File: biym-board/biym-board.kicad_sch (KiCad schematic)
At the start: 1 part

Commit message: Add driver external components
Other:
- sheet motor_driver ports: added ~{FAULT}; removed none
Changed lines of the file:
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@@
+    (stroke (width 0) (type default) (color 0 0 0 0))
+  )
+  (wire (pts (xy 217.17 100.33) (xy 214.63 100.33))
     (stroke (width 0) (type default) (color 0 0 0 0))
   )
@@
     (stroke (width 0) (type default) (color 0 0 0 0))
   )
+  (wire (pts (xy 182.88 102.87) (xy 180.34 102.87))
+    (stroke (width 0) (type default) (color 0 0 0 0))
+  )
   (wire (pts (xy 214.63 71.12) (xy 217.17 71.12))
     (stroke (width 0) (type default) (color 0 0 0 0))
@@
     (stroke (width 0) (type default) (color 0 0 0 0))
   )
+  (wire (pts (xy 180.34 113.03) (xy 182.88 113.03))
+    (stroke (width 0) (type default) (color 0 0 0 0))
+  )
   (wire (pts (xy 92.71 100.33) (xy 95.25 100.33))
     (stroke (width 0) (type default) (color 0 0 0 0))
@@
     (stroke (width 0) (type default) (color 0 0 0 0))
   )
+  (wire (pts (xy 180.34 105.41) (xy 182.88 105.41))
+    (stroke (width 0) (type default) (color 0 0 0 0))
+  )
   (wire (pts (xy 180.34 95.25) (xy 182.88 95.25))
     (stroke (width 0) (type default) (color 0 0 0 0))
@@
     (stroke (width 0) (type default) (color 0 0 0 0))
   )
+  (wire (pts (xy 180.34 107.95) (xy 182.88 107.95))
+    (stroke (width 0) (type default) (color 0 0 0 0))
+  )
   (wire (pts (xy 46.99 90.17) (xy 49.53 90.17))
     (stroke (width 0) (type default) (color 0 0 0 0))
@@
     (effects (font (size 1.27 1.27)) (justify right bottom))
   )
+  (label "DRIVER_PWM_A" (at 180.34 102.87 180)
+    (effects (font (size 1.27 1.27)) (justify right bottom))
+  )
   (label "GND" (at 46.99 95.25 180)
     (effects (font (size 1.27 1.27)) (justify right bottom))
@@
     (effects (font (size 1.27 1.27)) (justify right bottom))
   )
+  (label "~{DRIVER_FAULT}" (at 217.17 100.33 0)
+    (effects (font (size 1.27 1.27)) (justify left bottom))
+  )
   (label "VPERIPHERAL" (at 180.34 92.71 180)
     (effects (font (size 1.27 1.27)) (justify right bottom))
@@
     (effects (font (size 1.27 1.27)) (justify right bottom))
   )
+  (label "DRIVER_PWM_C" (at 180.34 107.95 180)
+    (effects (font (size 1.27 1.27)) (justify right bottom))
+  )
+  (label "DRIVER_PWM_B" (at 180.34 105.41 180)
+    (effects (font (size 1.27 1.27)) (justify right bottom))
+  )
   (label "~{DISABLE_ALL_POWER}" (at 95.25 100.33 0)
     (effects (font (size 1.27 1.27)) (justify left bottom))
+  )
+  (label "~{DRIVER_SLEEP}" (at 180.34 113.03 180)
+    (effects (font (size 1.27 1.27)) (justify right bottom))
   )
   (label "GND" (at 180.34 97.79 180)
@@
       (effects (font (size 1.27 1.27)) (justify left))
     )
-    (pin "PWM_B" input (at 182.88 102.87 180)
-      (effects (font (size 1.27 1.27)) (justify left))
-    )
-    (pin "PWM_A" input (at 182.88 105.41 180)
+    (pin "PWM_B" input (at 182.88 105.41 180)
+      (effects (font (size 1.27 1.27)) (justify left))
+    )
+    (pin "PWM_A" input (at 182.88 102.87 180)
       (effects (font (size 1.27 1.27)) (justify left))
     )
@@
     (pin "VDRIVER" passive (at 182.88 92.71 180)
       (effects (font (size 1.27 1.27)) (justify left))
+    )
+    (pin "~{FAULT}" output (at 214.63 100.33 0)
+      (effects (font (size 1.27 1.27)) (justify right))
     )
   )
@@
   )
   (symbol_instances
+    (path "/79116d11-26fd-48fc-b8f9-7a7b774125a1/2410a940-529b-42ac-a1a6-8eac39bf35e6"
+      (reference "C1") (unit 1) (value "0.1uF") (footprint "Janelia:SM0402")
+    )
+    (path "/79116d11-26fd-48fc-b8f9-7a7b774125a1/be9b6b49-dbbb-46e1-9161-07633a6035d9"
+      (reference "C2") (unit 1) (value "10uF") (footprint "Janelia:SM0402_POL")
+    )
+    (path "/79116d11-26fd-48fc-b8f9-7a7b774125a1/8a7cc49f-4666-4bff-88d8-7b1e5e0b9362"
+      (reference "C3") (unit 1) (value "0.1uF") (footprint "Janelia:SM0402")
+    )
+    (path "/79116d11-26fd-48fc-b8f9-7a7b774125a1/46ae94b0-5341-4bbb-afe7-3cf6a00b65a8"
+      (reference "C4") (unit 1) (value "0.1uF") (footprint "Janelia:SM0402")
+    )
+    (path "/79116d11-26fd-48fc-b8f9-7a7b774125a1/5df9f8b3-dc8a-4148-bf7f-d1adc6b6ce57"
+      (reference "C5") (unit 1) (value "10uF") (footprint "Janelia:SM0402_POL")
+    )
+    (path "/79116d11-26fd-48fc-b8f9-7a7b774125a1/a59ccd6c-12e8-44c6-9ed8-d91c4b04dd9f"
+      (reference "C6") (unit 1) (value "1uF") (footprint "Janelia:SM0402_POL")
+    )
+    (path "/79116d11-26fd-48fc-b8f9-7a7b774125a1/a44a33f9-40db-4e01-b1fe-0dfc38ff2344"
+      (reference "C7") (unit 1) (value "0.1uF") (footprint "Janelia:SM0402")
+    )
     (path "/78609776-14fe-41ec-972c-2bdc49eac818"
       (reference "FW1") (unit 1) (value "FEATHERWING_nRF52_POGO_PINS") (footprint "Janelia:FEATHERWING_POGO_PINS")
@@
     )
     (path "/79116d11-26fd-48fc-b8f9-7a7b774125a1/73049e1e-00b1-4d86-b27f-13c3a3887bed"
-      (reference "J?") (unit 1) (value "HEADER_01X03_JST_PH_VERTICAL") (footprint "Janelia:JST_PH_B3B-PH-K_1x03_P2.00mm_Vertical")
+      (reference "J2") (unit 1) (value "HEADER_01X03_JST_PH_VERTICAL") (footprint "Janelia:JST_PH_B3B-PH-K_1x03_P2.00mm_Vertical")
     )
     (path "/2c398cb1-cb17-49ba-86d6-22731656ead9/ab142e9c-269c-4749-bf0a-3cc0397cc4cb"
@@
       (reference "R1") (unit 1) (value "100k") (footprint "Janelia:SM0402")
     )
+    (path "/79116d11-26fd-48fc-b8f9-7a7b774125a1/922d9998-9360-4d64-bf82-803eb9724700"
+      (reference "R2") (unit 1) (value "5.1k") (footprint "Janelia:SM0402")
+    )
     (path "/79116d11-26fd-48fc-b8f9-7a7b774125a1/da95f1b2-1af2-47f6-bf0e-981916e2aac9"
-      (reference "U?") (unit 1) (value "DRV8311H") (footprint "Janelia:WQFN-24-1EP_3x3mm_P0.4mm_EP1.9x1.9mm_ThermalVias")
-    )
-  )
+      (reference "U1") (unit 1) (value "DRV8311H") (footprint "Janelia:WQFN-24-1EP_3x3mm_P0.4mm_EP1.9x1.9mm_ThermalVias")
+    )
+  )

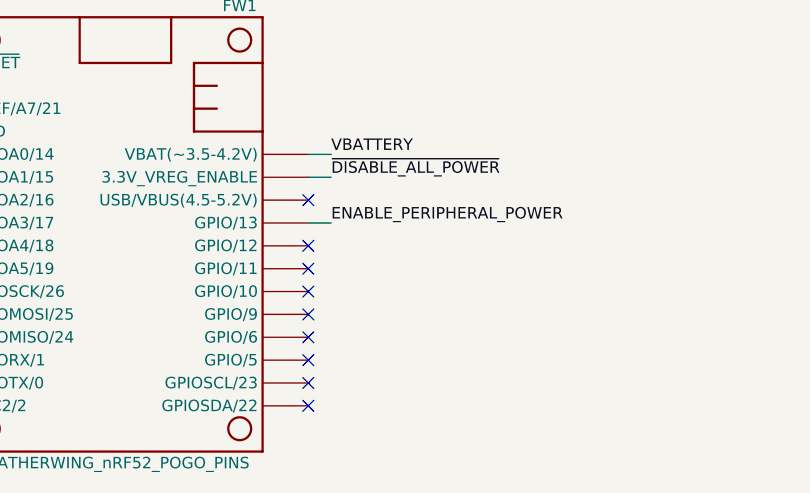
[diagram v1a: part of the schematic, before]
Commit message: Initial driver wiring
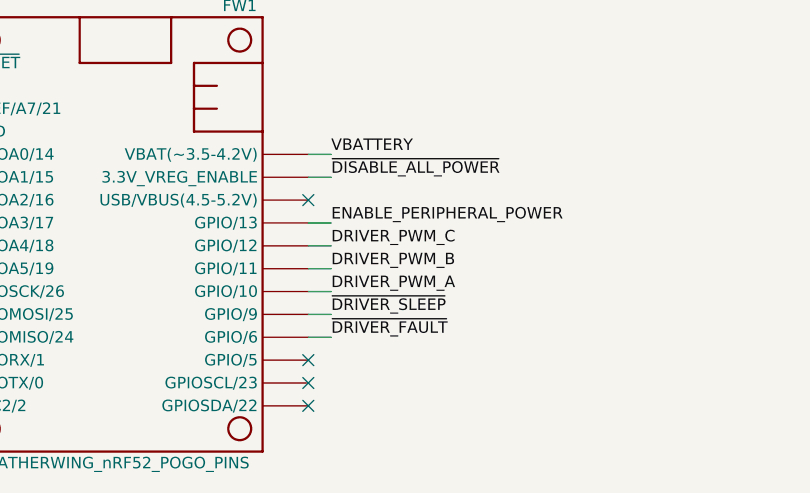
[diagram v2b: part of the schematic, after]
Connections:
- net DRIVER_PWM_A: now also FW1.22 (GPIO/10)
- net DRIVER_PWM_B: now also FW1.23 (GPIO/11)
- net DRIVER_PWM_C: now also FW1.24 (GPIO/12)
- net ~{DRIVER_FAULT}: now also FW1.20 (GPIO/6)
- net ~{DRIVER_SLEEP}: now also FW1.21 (GPIO/9)
- no-connect marks 23 -> 18
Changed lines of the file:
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@@
   (no_connect (at 49.53 92.71))
   (no_connect (at 49.53 123.19))
-  (no_connect (at 92.71 118.11))
   (no_connect (at 92.71 123.19))
   (no_connect (at 92.71 120.65))
@@
   (no_connect (at 49.53 87.63))
   (no_connect (at 49.53 113.03))
-  (no_connect (at 92.71 107.95))
-  (no_connect (at 92.71 110.49))
   (no_connect (at 49.53 120.65))
   (no_connect (at 49.53 105.41))
-  (no_connect (at 92.71 113.03))
   (no_connect (at 49.53 118.11))
   (no_connect (at 49.53 110.49))
-  (no_connect (at 92.71 115.57))
   (no_connect (at 92.71 102.87))
   (no_connect (at 49.53 102.87))
@@
     (stroke (width 0) (type default) (color 0 0 0 0))
   )
+  (wire (pts (xy 95.25 118.11) (xy 92.71 118.11))
+    (stroke (width 0) (type default) (color 0 0 0 0))
+  )
   (wire (pts (xy 92.71 105.41) (xy 95.25 105.41))
     (stroke (width 0) (type default) (color 0 0 0 0))
@@
     (stroke (width 0) (type default) (color 0 0 0 0))
   )
+  (wire (pts (xy 95.25 110.49) (xy 92.71 110.49))
+    (stroke (width 0) (type default) (color 0 0 0 0))
+  )
   (wire (pts (xy 214.63 71.12) (xy 217.17 71.12))
     (stroke (width 0) (type default) (color 0 0 0 0))
@@
     (stroke (width 0) (type default) (color 0 0 0 0))
   )
+  (wire (pts (xy 95.25 115.57) (xy 92.71 115.57))
+    (stroke (width 0) (type default) (color 0 0 0 0))
+  )
   (wire (pts (xy 180.34 105.41) (xy 182.88 105.41))
     (stroke (width 0) (type default) (color 0 0 0 0))
@@
     (stroke (width 0) (type default) (color 0 0 0 0))
   )
+  (wire (pts (xy 92.71 113.03) (xy 95.25 113.03))
+    (stroke (width 0) (type default) (color 0 0 0 0))
+  )
   (wire (pts (xy 180.34 107.95) (xy 182.88 107.95))
     (stroke (width 0) (type default) (color 0 0 0 0))
   )
+  (wire (pts (xy 92.71 107.95) (xy 95.25 107.95))
+    (stroke (width 0) (type default) (color 0 0 0 0))
+  )
   (wire (pts (xy 46.99 90.17) (xy 49.53 90.17))
     (stroke (width 0) (type default) (color 0 0 0 0))
   )
+  (label "~{DRIVER_FAULT}" (at 95.25 118.11 0)
+    (effects (font (size 1.27 1.27)) (justify left bottom))
+  )
   (label "ENABLE_PERIPHERAL_POWER" (at 95.25 105.41 0)
     (effects (font (size 1.27 1.27)) (justify left bottom))
@@
     (effects (font (size 1.27 1.27)) (justify right bottom))
   )
+  (label "DRIVER_PWM_B" (at 95.25 110.49 0)
+    (effects (font (size 1.27 1.27)) (justify left bottom))
+  )
   (label "GND" (at 46.99 95.25 180)
     (effects (font (size 1.27 1.27)) (justify right bottom))
@@
     (effects (font (size 1.27 1.27)) (justify right bottom))
   )
+  (label "DRIVER_PWM_C" (at 95.25 107.95 0)
+    (effects (font (size 1.27 1.27)) (justify left bottom))
+  )
+  (label "~{DRIVER_SLEEP}" (at 95.25 115.57 0)
+    (effects (font (size 1.27 1.27)) (justify left bottom))
+  )
   (label "~{DRIVER_FAULT}" (at 217.17 100.33 0)
     (effects (font (size 1.27 1.27)) (justify left bottom))
@@
   (label "VPERIPHERAL" (at 180.34 92.71 180)
     (effects (font (size 1.27 1.27)) (justify right bottom))
+  )
+  (label "DRIVER_PWM_A" (at 95.25 113.03 0)
+    (effects (font (size 1.27 1.27)) (justify left bottom))
   )
   (label "~{DISABLE_ALL_POWER}" (at 217.17 71.12 0)
@@
   )
   (symbol_instances
+    (path "/2c398cb1-cb17-49ba-86d6-22731656ead9/8e033e98-a73f-4e07-b564-ba8f1320f212"
+      (reference "#FLG0101") (unit 1) (value "PWR_FLAG") (footprint "")
+    )
     (path "/79116d11-26fd-48fc-b8f9-7a7b774125a1/2410a940-529b-42ac-a1a6-8eac39bf35e6"
       (reference "C1") (unit 1) (value "0.1uF") (footprint "Janelia:SM0402")

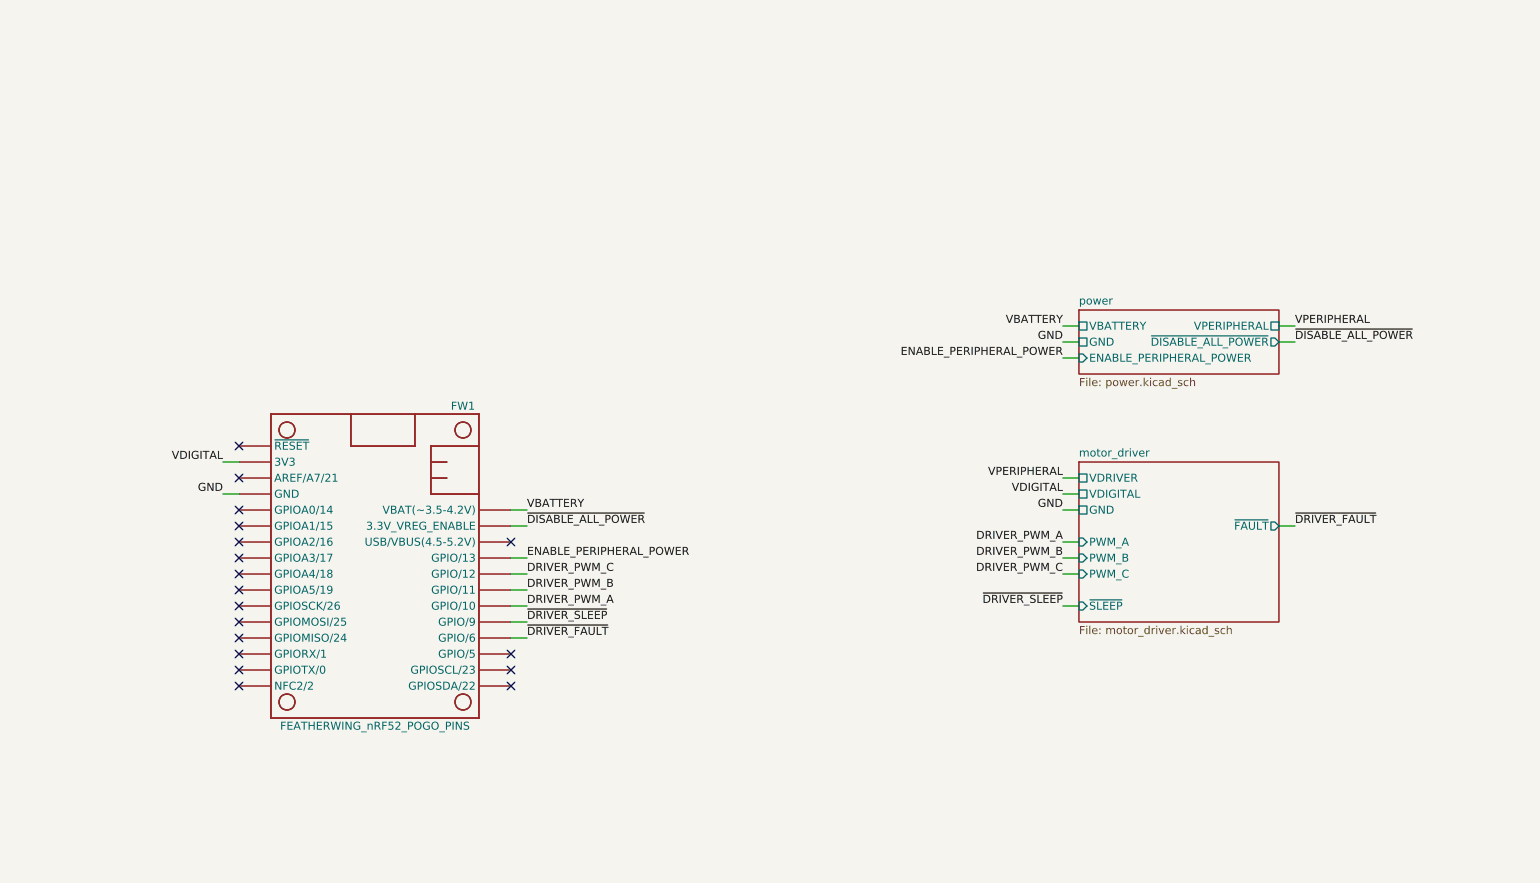
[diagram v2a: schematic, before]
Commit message: Add motor feedback
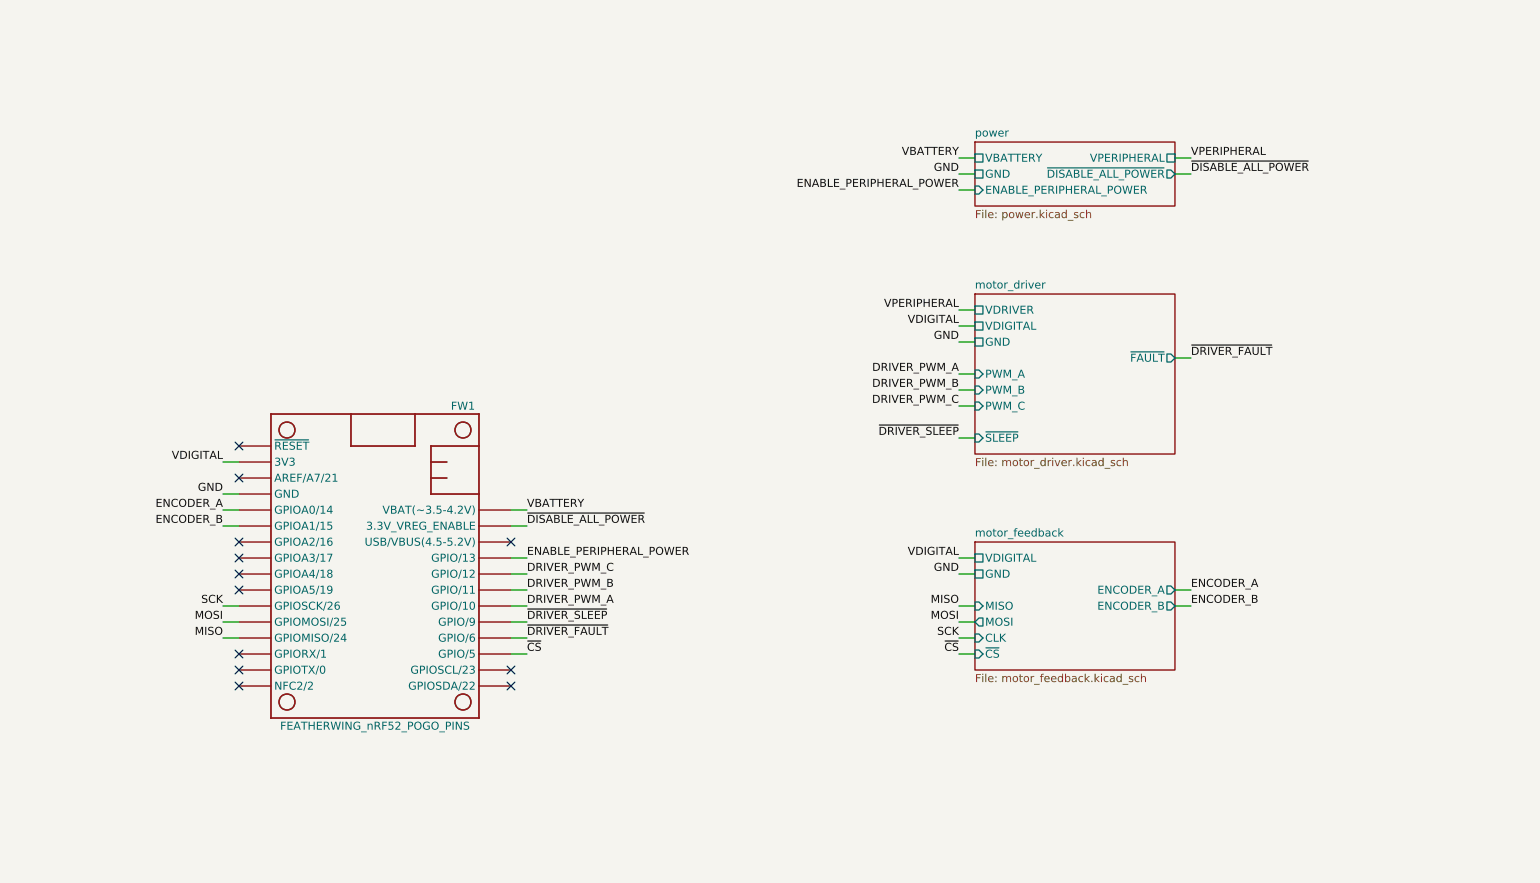
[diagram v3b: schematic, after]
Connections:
- net SCK: now reaches FW1.11 (GPIOSCK/26)
- net MOSI: now reaches FW1.12 (GPIOMOSI/25)
- net MISO: now reaches FW1.13 (GPIOMISO/24)
- net ~{CS}: now reaches FW1.19 (GPIO/5)
- net ENCODER_A: now reaches FW1.5 (GPIOA0/14)
- net ENCODER_B: now reaches FW1.6 (GPIOA1/15)
- no-connect marks 18 -> 12
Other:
- added sheet motor_feedback (motor_feedback.kicad_sch)

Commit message: Rename sheets
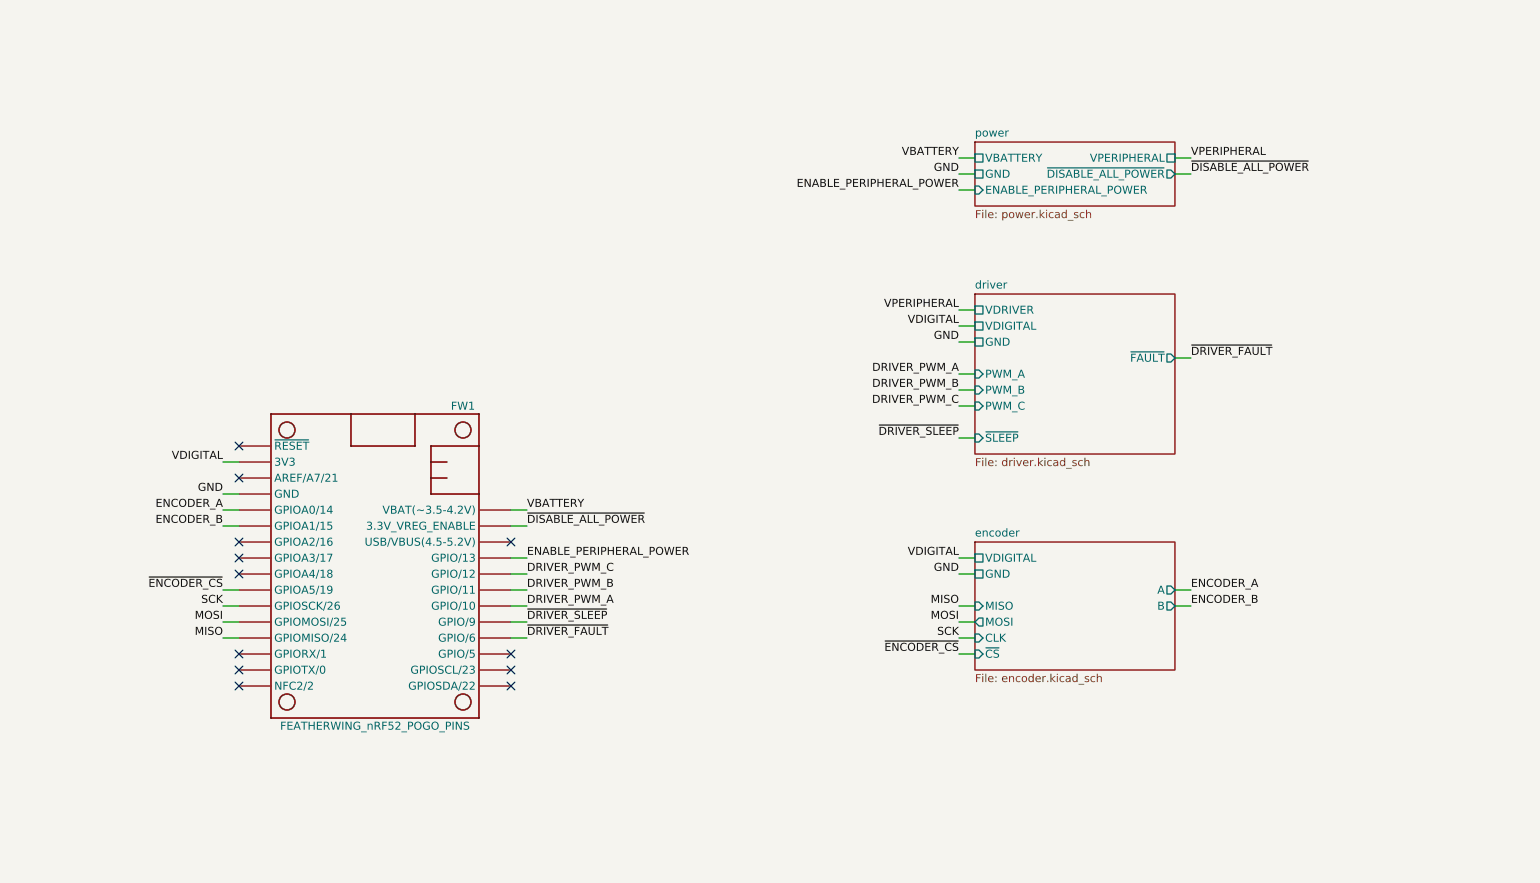
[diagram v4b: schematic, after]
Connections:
- net ~{ENCODER_CS}: now reaches FW1.10 (GPIOA5/19)
- net ~{CS}: no longer names the net of FW1.19 (GPIO/5)
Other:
- sheet motor_driver renamed driver
- sheet motor_feedback renamed encoder
- sheet driver: file motor_driver.kicad_sch -> driver.kicad_sch
- sheet encoder: file motor_feedback.kicad_sch -> encoder.kicad_sch
- sheet encoder ports: added A, B; removed ENCODER_A, ENCODER_B
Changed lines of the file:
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@@
   (no_connect (at 49.53 92.71))
   (no_connect (at 49.53 123.19))
+  (no_connect (at 92.71 120.65))
   (no_connect (at 92.71 123.19))
   (no_connect (at 49.53 125.73))
@@
   (no_connect (at 49.53 120.65))
   (no_connect (at 49.53 105.41))
-  (no_connect (at 49.53 110.49))
   (no_connect (at 92.71 102.87))
   (no_connect (at 49.53 102.87))
@@
     (stroke (width 0) (type default) (color 0 0 0 0))
   )
-  (wire (pts (xy 95.25 120.65) (xy 92.71 120.65))
+  (wire (pts (xy 46.99 110.49) (xy 49.53 110.49))
     (stroke (width 0) (type default) (color 0 0 0 0))
   )
@@
     (effects (font (size 1.27 1.27)) (justify right bottom))
   )
-  (label "~{CS}" (at 163.83 120.65 180)
+  (label "~{ENCODER_CS}" (at 163.83 120.65 180)
     (effects (font (size 1.27 1.27)) (justify right bottom))
   )
@@
     (effects (font (size 1.27 1.27)) (justify left bottom))
   )
-  (label "~{CS}" (at 95.25 120.65 0)
-    (effects (font (size 1.27 1.27)) (justify left bottom))
+  (label "~{ENCODER_CS}" (at 46.99 110.49 180)
+    (effects (font (size 1.27 1.27)) (justify right bottom))
   )
   (symbol (lib_id "Janelia:FEATHERWING_nRF52_POGO_PINS") (at 71.12 106.68 0) (unit 1)
@@
     (stroke (width 0.1524) (type solid) (color 0 0 0 0))
     (fill (color 0 0 0 0.0000))
-    (property "Sheet name" "motor_feedback" (id 0) (at 166.37 102.1584 0)
+    (property "Sheet name" "encoder" (id 0) (at 166.37 102.1584 0)
       (effects (font (size 1.27 1.27)) (justify left bottom))
     )
-    (property "Sheet file" "motor_feedback.kicad_sch" (id 1) (at 166.37 123.7746 0)
+    (property "Sheet file" "encoder.kicad_sch" (id 1) (at 166.37 123.7746 0)
       (effects (font (size 1.27 1.27)) (justify left top))
     )
@@
       (effects (font (size 1.27 1.27)) (justify left))
     )
-    (pin "ENCODER_A" output (at 198.12 110.49 0)
+    (pin "A" output (at 198.12 110.49 0)
       (effects (font (size 1.27 1.27)) (justify right))
     )
-    (pin "ENCODER_B" output (at 198.12 113.03 0)
+    (pin "B" output (at 198.12 113.03 0)
       (effects (font (size 1.27 1.27)) (justify right))
     )
@@
     (stroke (width 0.1524) (type solid) (color 0 0 0 0))
     (fill (color 0 0 0 0.0000))
-    (property "Sheet name" "motor_driver" (id 0) (at 166.37 62.7884 0)
+    (property "Sheet name" "driver" (id 0) (at 166.37 62.7884 0)
       (effects (font (size 1.27 1.27)) (justify left bottom))
     )
-    (property "Sheet file" "motor_driver.kicad_sch" (id 1) (at 166.37 89.4846 0)
+    (property "Sheet file" "driver.kicad_sch" (id 1) (at 166.37 89.4846 0)
       (effects (font (size 1.27 1.27)) (justify left top))
     )
